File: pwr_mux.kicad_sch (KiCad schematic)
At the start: 14 parts, among them Q1 SIR5607DP-T1-RE3, Q2 SSM3K7002KFU,LF, Q3 SSM3K7002KFU,LF, Q4 SIR5607DP-T1-RE3, Q5 SSM3K7002KFU,LF, Q6 SSM3K7002KFU,LF, Q7 SIR5607DP-T1-RE3, Q8 SIR5607DP-T1-RE3

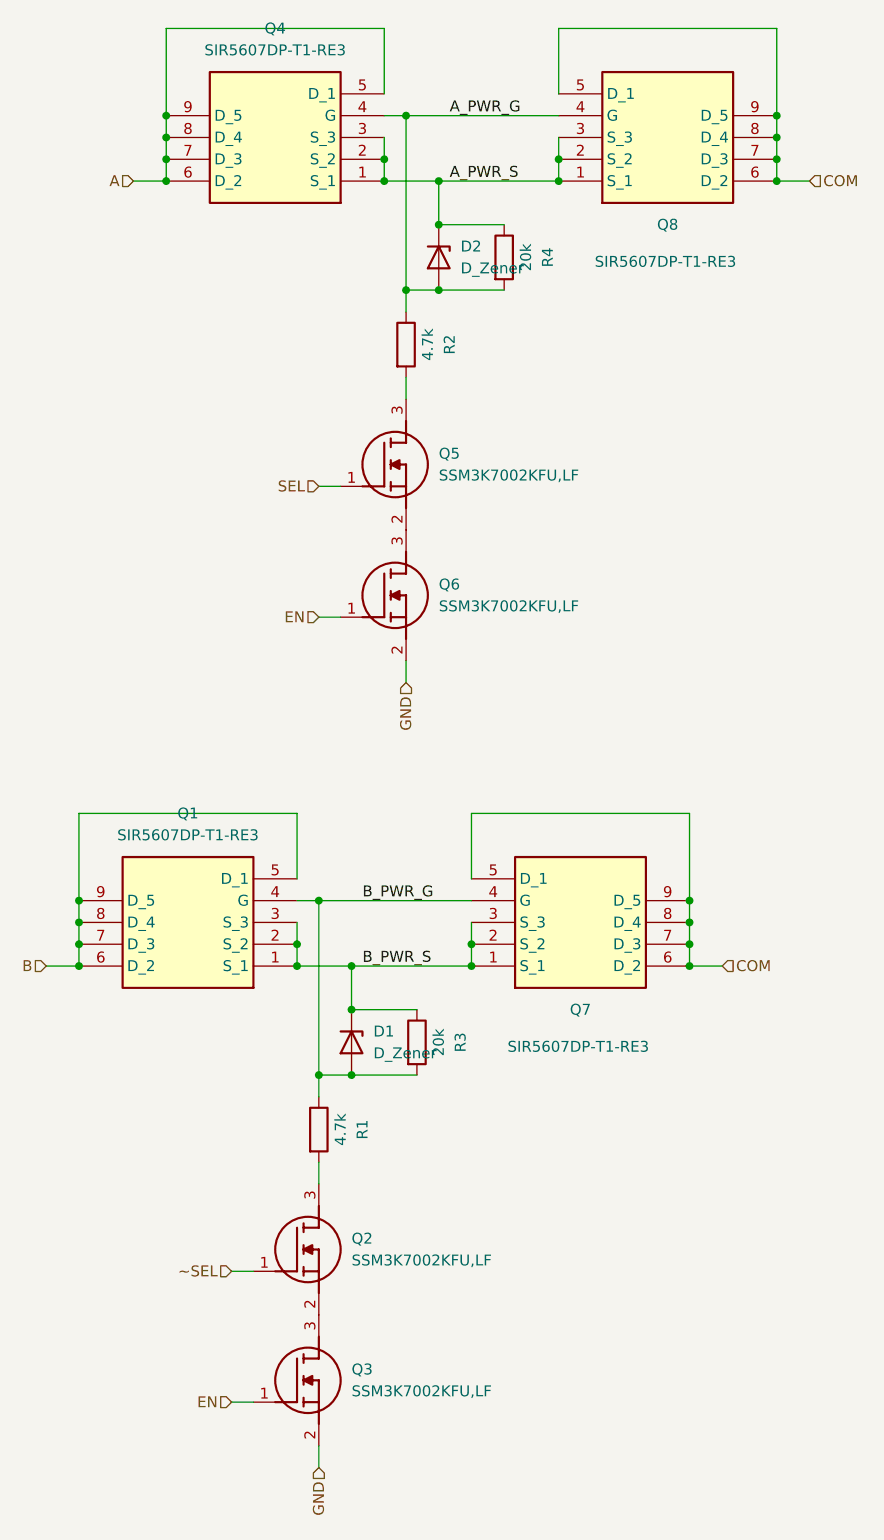
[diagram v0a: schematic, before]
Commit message: add capacitors, move B pwr control, select remaining components
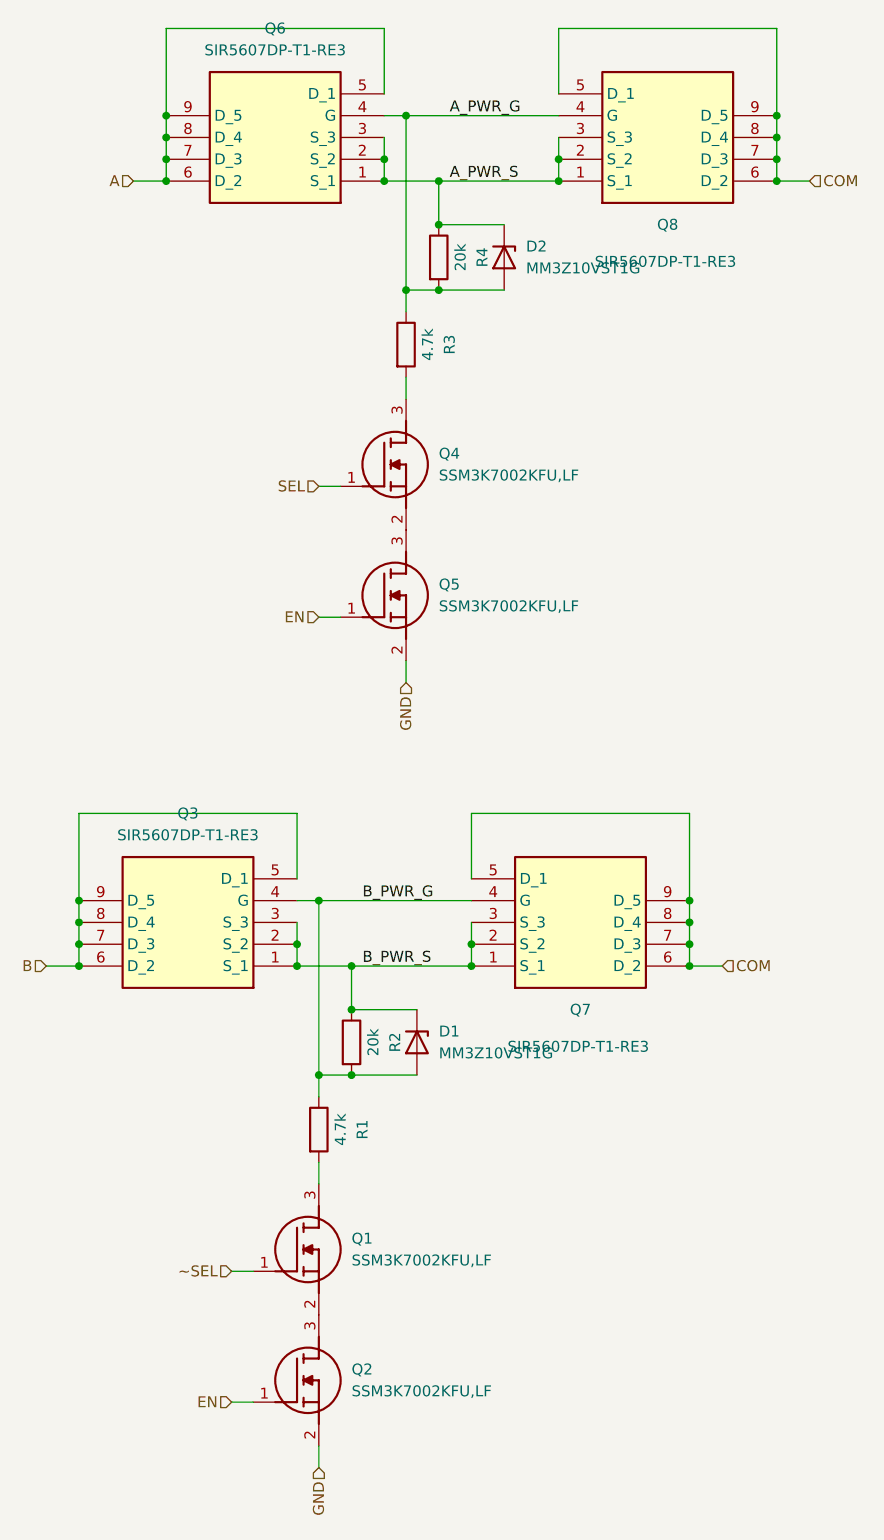
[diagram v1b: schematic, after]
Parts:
- D1, D2: value D_Zener -> MM3Z10VST1G; footprint Diode_SMD:D_0402_1005Metric -> Diode_SMD:D_SOD-323
- renumbered Q2 to Q1, Q3 to Q2, Q1 to Q3, Q5 to Q4, Q6 to Q5, Q4 to Q6, R3 to R2, R2 to R3
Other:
- moved on the sheet: D1, D2, R2, R4
